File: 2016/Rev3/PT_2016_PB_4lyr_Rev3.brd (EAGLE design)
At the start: 153.9 x 200.4 mm, 178 parts, among them Q12 2N7002

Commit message: Changed board to 3.3v, added 12v buck protection
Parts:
- removed 1M: 10kΩ, resistor:R1206
- removed 9.31M: 60kΩ, resistor:R1206
- removed R12, R16, R18, R20, R22, R24, R26, R28, R29: 249k, SparkFun-Resistors:1206
- removed R14, R17, R19, R21, R23, R25, R27, R30, R31, R9: 499k, SparkFun-Resistors:1206
- removed REY-5V: MURATA_5V_DC-DC_CONVERTER, MRDT-2015-PowerBoard:MURATA_5V_DC-DC_CONVERTER@1
- added BB-8-5V1: Q_OKI-78SR, MRDT-2015-PowerBoard:OKI-78SR_HORIZ
- added C10, C9: 1uF, resistor:C1206
- added C5: 1nF, resistor:C1206
- added C7: 10uF, resistor:C1206
- added C8: .1uF, resistor:C1206
- added Q1, Q3: Q_IRF7437SMD, MRDT-2015-PowerBoard:D2PACK
- added Q2: 2N7002, SparkFun-DiscreteSemi:SOT323
- added R3: 100k 1%, resistor:R1206
- added R4: 10kΩ 1%, resistor:R1206
- added U$13, U$9: LM74670-Q1, LM74670-Q1:LM74670-Q1
- added U$7: UVQ-5/20-D24PB-C, MRDT-2015-PowerBoard:MURATA_5V_DC-DC_CONVERTER
- BB-8-5V: device MRDT-2015-PowerBoard:OKI-78SRH -> MRDT-2015-PowerBoard:OKI-78SR_HORIZ
- R5: value 249k -> 1k; device SparkFun-Resistors:1206 -> resistor:R1206
- moved R5 79.7 mm to (129.3, 145.0)
- moved C2 22.3 mm to (59.4, 73.7)
- moved C46 19.6 mm to (62.0, 139.2)
- moved C3 19.1 mm to (59.4, 59.9)
- moved C45 8.07 mm to (79.7, 139.2)
- moved C13 7.62 mm to (89.4, 166.1)
- moved C14 7.62 mm to (71.6, 166.1)
- moved C15 7.62 mm to (81.8, 166.1)
- moved C34 7.62 mm to (76.7, 166.1)
- moved C44 7.62 mm to (66.5, 166.1)
- moved C52 7.62 mm to (69.1, 166.1)
- moved C53 7.62 mm to (86.9, 166.1)
- moved C17 7.62 mm to (84.3, 166.1)
- moved C50 7.62 mm to (79.2, 166.1)
- moved C51 7.62 mm to (74.2, 166.1)
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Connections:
- removed net +5V: 5V-INT.R, ACS714-M1.8, ACS714-M2.8, ACS714-M3.8, ACS714-M4.8, ACS714-M5.8, ACS714-M6.8, ACS714-M7.8, ACS714-M8.8, ACS714CAP-M1.2, ACS714CAP-M2.2, ACS714CAP-M3.2, ACS714CAP-M4.2, ACS714CAP-M5.2, ACS714CAP-M6.2, ACS714CAP-M7.2, ACS714CAP-M8.2, BB-8-5V.3, C11.2, C47.1, C48.1, C49.1, C6.2, LED5.A, U$1.+5V_1, U$1.+5V_2, U$12.VCC, U$21.8, U$24.VCC, U$3.8
- removed net IMEAS-12VR: R29.1, U$21.7
- removed net IMEAS-5VR: R28.1, U$3.7
- removed net IMEAS-M1R: ACS714-M1.7, R18.1
- removed net IMEAS-M2R: ACS714-M2.7, R16.1
- removed net IMEAS-M3R: ACS714-M3.7, R12.1
- removed net IMEAS-M4R: ACS714-M4.7, R5.1
- removed net IMEAS-M5R: ACS714-M5.7, R20.1
- removed net IMEAS-M6R: ACS714-M6.7, R26.1
- removed net IMEAS-M7R: ACS714-M7.7, R24.1
- removed net IMEAS-M8R: ACS714-M8.7, R22.1
- new net 3.3V: 5V-INT.R, ACS714-M1.8, ACS714-M2.8, ACS714-M3.8, ACS714-M4.8, ACS714-M5.8, ACS714-M6.8, ACS714-M7.8, ACS714-M8.8, ACS714CAP-M1.2, ACS714CAP-M2.2, ACS714CAP-M3.2, ACS714CAP-M4.2, ACS714CAP-M5.2, ACS714CAP-M6.2, ACS714CAP-M7.2, ACS714CAP-M8.2, BB-8-5V.3, C11.2, C47.1, C48.1, C49.1, C6.2, LED5.A, U$12.VCC, U$21.8, U$24.VCC, U$3.8
- new net 5V: BB-8-5V1.3, C5.1, C7.1, C8.1, U$1.+5V_1, U$1.+5V_2
- new net N$1: FINN-12V.8, Q3.2, U$9.P$8
- new net N$10: C10.2, U$13.P$5
- new net N$2: POE-12V.8, Q1.2, U$13.P$8
- new net N$3: Q3.1, U$9.P$3, U$9.P$6
- new net N$48: Q2.1, R11.1
- new net N$5: Q1.1, U$13.P$3, U$13.P$6
- new net N$7: C9.1, U$9.P$2
- new net N$8: C9.2, U$9.P$5
- new net N$9: C10.1, U$13.P$2
- net GND: now also BB-8-5V1.2, C5.2, C7.2, C8.2, Q2.2, R4.1, R5.2, U$7.P$3, U$7.P$6, U$7.P$7; no longer 1M.1, R14.1, R17.1, R19.1, R21.1, R23.1, R25.1, R27.1, R30.1, R31.1, R9.1, REY-5V.P$2, REY-5V.P$5, REY-5V.P$8
- net IMEAS-12V: now also U$21.7; no longer R29.2, R30.2
- net IMEAS-5V: now also U$1.PE2, U$3.7; no longer R28.2, R31.2, U$1.PE3
- net IMEAS-M1: now also ACS714-M1.7; no longer R18.2, R19.2
- net IMEAS-M2: now also ACS714-M2.7; no longer R16.2, R17.2
- net IMEAS-M3: now also ACS714-M3.7; no longer R12.2, R14.2
- net IMEAS-M4: now also ACS714-M4.7; no longer R5.2, R9.2
- net IMEAS-M5: now also ACS714-M5.7; no longer R20.2, R21.2
- net IMEAS-M6: now also ACS714-M6.7; no longer R26.2, R27.2
- net IMEAS-M7: now also ACS714-M7.7; no longer R24.2, R25.2
- net IMEAS-M8: now also ACS714-M8.7; no longer R22.2, R23.2
- net N$114: now also R5.1
- net N$33: now also Q1.TAB, Q3.TAB, U$13.P$1, U$9.P$1; no longer FINN-12V.8, POE-12V.8
- net N$43: now also Q2.3, U$7.P$1; no longer R11.1, REY-5V.P$1
- net N$71: now also U$7.P$5, U$7.P$8; no longer REY-5V.P$6, REY-5V.P$7
- net VMEAS-VBATT: now also R3.1, R4.2, U$1.PE3; no longer 1M.2, 9.31M.1, U$1.PE2
- net V_BATT: now also BB-8-5V1.1, R3.2, U$7.P$2; no longer 9.31M.2, REY-5V.P$3
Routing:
- net IMEAS-M1: track 11.3 -> 238.8 mm
- net IMEAS-M1R: track 224.7 -> 0.00 mm, vias 2 -> 0
- net IMEAS-M2: track 14.7 -> 220.9 mm
- net IMEAS-M2R: track 202.7 -> 0.00 mm, vias 2 -> 0
- net IMEAS-M3: track 18.0 -> 204.7 mm
- net IMEAS-M3R: track 182.5 -> 0.00 mm, vias 2 -> 0
- net IMEAS-M4: track 23.9 -> 190.8 mm
- net IMEAS-M4R: track 162.0 -> 0.00 mm, vias 2 -> 0
- net 5V: track 0.00 -> 151.0 mm
- net IMEAS-M5: track 23.6 -> 170.1 mm
- net IMEAS-M5R: track 141.2 -> 0.00 mm, vias 2 -> 0
- net IMEAS-M6: track 27.0 -> 153.9 mm
- net IMEAS-M6R: track 121.2 -> 0.00 mm, vias 2 -> 0
- net IMEAS-M7: track 30.3 -> 138.3 mm
- net IMEAS-M7R: track 101.6 -> 0.00 mm, vias 2 -> 0
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- added copper zone on layer 1, net 3.3V
- added copper zone on layer 2, net 3.3V
- added copper zone on layer 1, net 5V
- removed copper zone on layer 1, net +5V
- removed copper zone on layer 2, net +5V
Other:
- board size 153.9 x 200.4 mm -> 155.7 x 202.7 mm

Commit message: Moved around 12v bucks, routed ORing mosfet circuits
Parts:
- removed R1, R6: 120 Ohm, SparkFun-Passives:1206
- removed U$12: MAX3077, MAX3077:MAX3070E
- removed U$6: RJ45FCI-54602-908LF, MRDT-2015-General:FCI-54602-908LF
- moved C9 213.9 mm to (111.0, 97.0), turned to 270 degrees
- moved C10 201.7 mm to (86.6, 97.0), turned to 270 degrees
- moved U$13 195.8 mm to (89.7, 97.5)
- moved Q1 187.6 mm to (102.6, 97.5), turned to 270 degrees
- moved Q3 186.4 mm to (127.0, 97.5), turned to 270 degrees
- moved U$9 173.0 mm to (114.0, 97.5)
- moved C19 52.9 mm to (97.3, 88.4), flipped to the top, turned to 0 degrees
- moved C47 47.2 mm to (90.9, 112.3), turned to 0 degrees
- moved C49 46.5 mm to (90.9, 109.7), turned to 0 degrees
- moved C48 46.1 mm to (90.9, 107.2), turned to 0 degrees
- moved U$5 44.8 mm to (151.4, 96.3)
- moved BB-8-5V 36.8 mm to (86.1, 112.3), turned to 90 degrees
- moved FINN-12V 31.4 mm to (135.8, 57.4), turned to 90 degrees
- moved C5 26.4 mm to (90.9, 124.0), turned to 0 degrees
- moved C8 25.7 mm to (90.9, 121.4), turned to 0 degrees
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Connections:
- removed net REC+: R1.1, U$12.A, U$6.1
- removed net REC-: R1.2, U$12.B, U$6.2
- removed net TRANS+: R6.2, U$12.Y, U$6.3
- removed net TRANS-: R6.1, U$12.Z, U$6.6
- net 3.3V: no longer 5V-INT.R, LED5.A, U$12.VCC
- net 5V: now also 5V-INT.R, LED5.A
- net GND: no longer U$12.GND, U$6.7, U$6.8
- net N$1: now also C20.1
- net N$2: now also C19.1
- net N$33: no longer C19.1, C20.1
- net RX2: no longer U$12.RO
- net TX2: no longer U$12.DI
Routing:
- net 5V: track 151.0 -> 334.1 mm
- net TRANS+: track 175.1 -> 0.00 mm, vias 1 -> 0
- net REC+: track 168.4 -> 0.00 mm, vias 1 -> 0
- net REC-: track 165.6 -> 0.00 mm, vias 1 -> 0
- net TRANS-: track 160.4 -> 0.00 mm, vias 1 -> 0
- net N$4: track 146.6 -> 0.00 mm, vias 2 -> 0
- net N$43: track 53.0 -> 0.00 mm, vias 2 -> 0
- net TRANS+1: track 150.7 -> 109.2 mm
- net TX2: track 36.6 -> 0.00 mm
- net TRANS-1: track 141.0 -> 104.4 mm
- net RX2: track 34.9 -> 0.00 mm
- net REC+1: track 151.4 -> 117.1 mm
- net REC-1: track 146.7 -> 116.8 mm
- net N$33: track 158.7 -> 183.8 mm
- net N$5: track 0.00 -> 10.3 mm
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- added copper zone on layer 1, net N$1
- added copper zone on layer 1, net N$2
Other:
- board text added: "ZENITH"

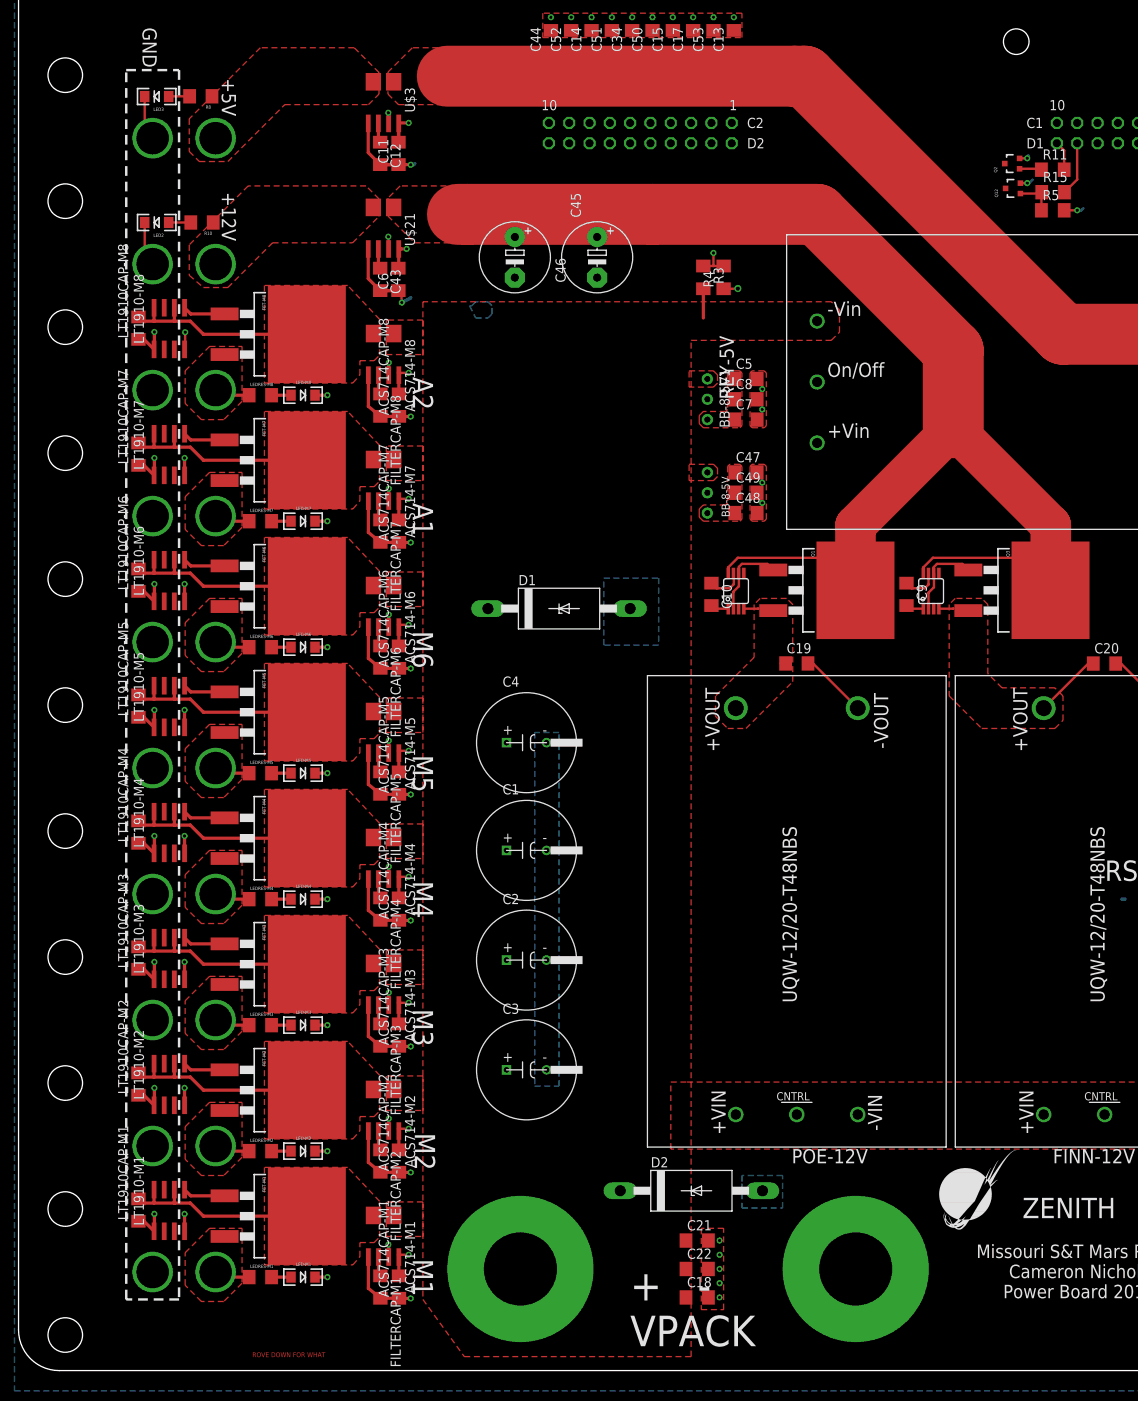
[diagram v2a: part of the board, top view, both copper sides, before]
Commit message: Updated part sizes
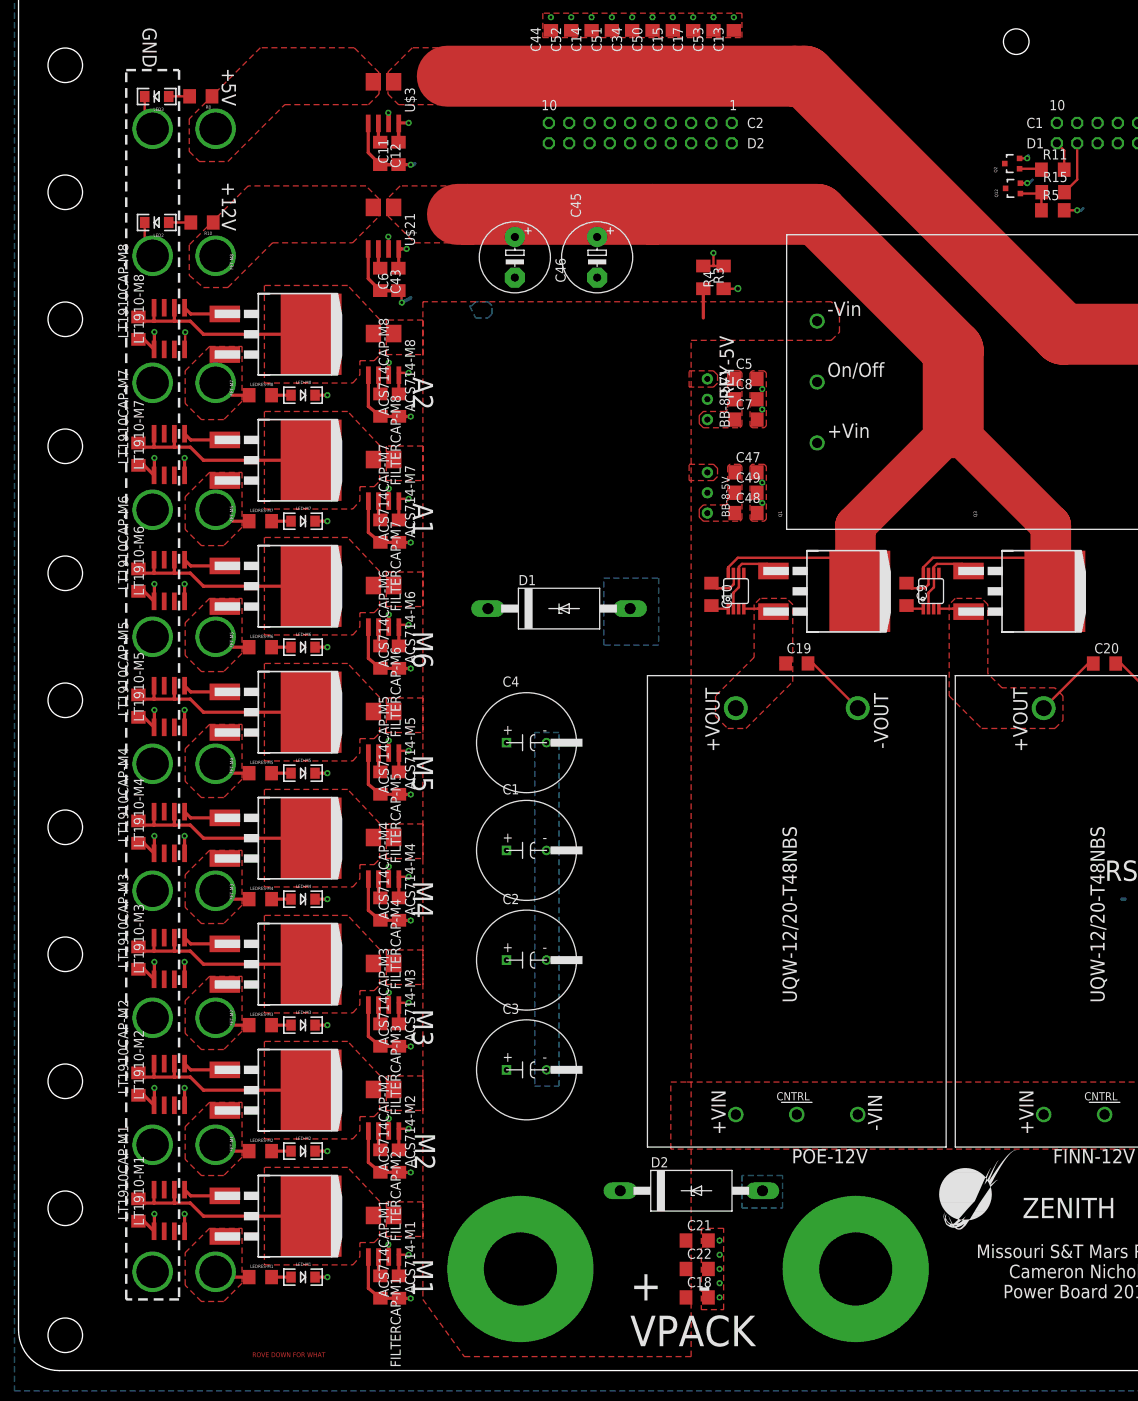
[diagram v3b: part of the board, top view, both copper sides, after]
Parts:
- BOTAPP-M1, BOTAPP-M2, BOTAPP-M3, BOTAPP-M4, BOTAPP-M5, BOTAPP-M6, BOTAPP-M7, BOTAPP-M8, U$28, U$29: value ANDERSON_POWERPOLEPP45_PCB_HORIZ_RIGHT -> APPPP45_PCB_HORIZ_RIGHT
- TOPAPP-M1, TOPAPP-M2, TOPAPP-M3, TOPAPP-M4, TOPAPP-M5, TOPAPP-M6, TOPAPP-M7, TOPAPP-M8, U$26, U$27: value ANDERSON_POWERPOLEPP45_PCB_HORIZ_RIGHT_2HIGH -> APPPP45_PCB_HORIZ_RIGHT_2HIGH
- moved FET-M8 6.51 mm to (30.0, 134.6)
- moved FET-M3 6.51 mm to (30.0, 55.9)
- moved FET-M1 6.51 mm to (30.0, 24.4)
- moved FET-M2 6.51 mm to (30.0, 40.1)
- moved FET-M4 6.51 mm to (30.0, 71.6)
- moved FET-M5 6.51 mm to (30.0, 87.4)
- moved FET-M6 6.51 mm to (30.0, 103.1)
- moved FET-M7 6.51 mm to (30.0, 118.9)
- moved Q1 6.41 mm to (98.6, 102.5)
- moved Q3 6.41 mm to (122.9, 102.5)
- moved U$25 1.27 mm to (13.2, 167.1)
- moved U$27 1.14 mm to (-11.4, 151.3)
- moved U$28 1.14 mm to (-11.4, 151.3)
- moved U$41 1.14 mm to (13.2, 151.3)
- moved U$26 1.02 mm to (-11.4, 135.4)
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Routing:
- net N$33: track 183.8 -> 181.3 mm
- net GND: track 194.9 -> 192.7 mm
- net SOURCE-M8: track 4.82 -> 5.74 mm
- net SOURCE-M7: track 4.82 -> 5.62 mm
- net SOURCE-M6: track 4.82 -> 5.49 mm
- net DRAIN-M8: track 25.5 -> 26.0 mm
- net DRAIN-M7: track 25.5 -> 26.0 mm
- net DRAIN-M6: track 25.5 -> 26.0 mm
- net DRAIN-M5: track 25.5 -> 26.0 mm
- net DRAIN-M4: track 25.5 -> 26.0 mm
- net DRAIN-M3: track 25.5 -> 26.0 mm
- net DRAIN-M2: track 25.5 -> 26.0 mm
- net DRAIN-M1: track 25.5 -> 26.0 mm
- net SOURCE-M5: track 4.82 -> 5.36 mm
